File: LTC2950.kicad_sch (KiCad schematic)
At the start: 21 parts, among them SW1 SW_Push, U2 LTC2950ITS8-2_TRMPBF

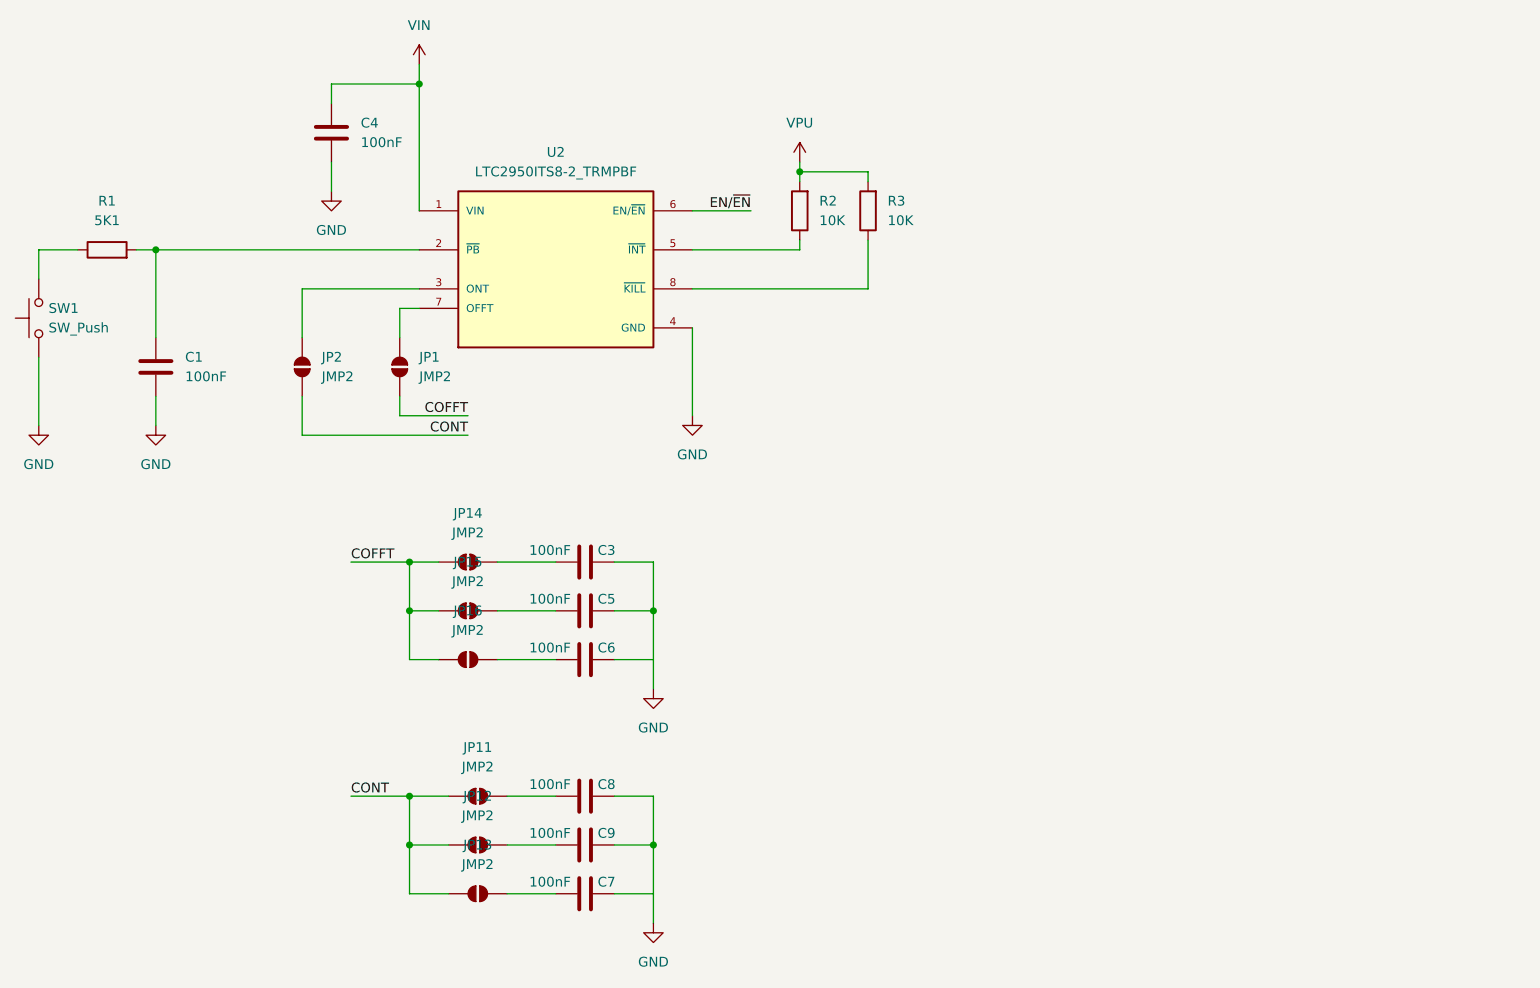
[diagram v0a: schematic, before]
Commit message: Added B.O.M, TODO: do PCB track layout
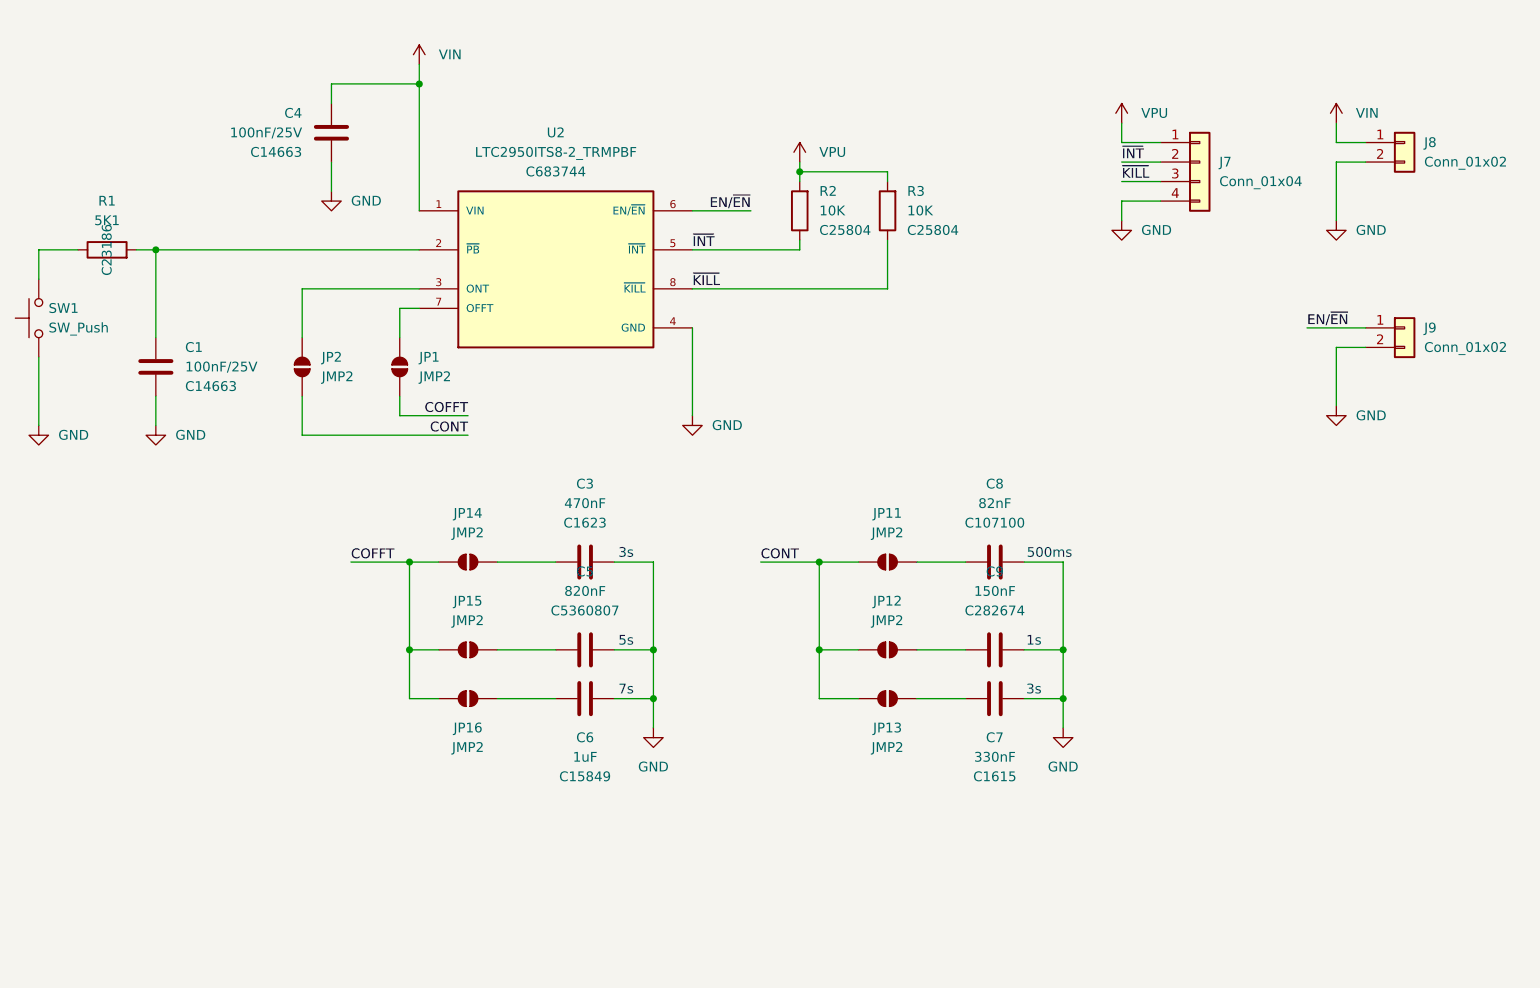
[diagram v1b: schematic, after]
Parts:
- added J7: Conn_01x04, Connector_PinHeader_2.54mm:PinHeader_1x04_P2.54mm_Vertical, symbol Connector_Generic:Conn_01x04
- added J8, J9: Conn_01x02, Connector_PinHeader_2.54mm:PinHeader_1x02_P2.54mm_Vertical, symbol Connector_Generic:Conn_01x02
- C1, C4: value 100nF -> 100nF/25V; JLCPCB Part # (none) -> C14663
- C3: value 100nF -> 470nF; JLCPCB Part # (none) -> C1623
- C5: value 100nF -> 820nF; JLCPCB Part # (none) -> C5360807
- C6: value 100nF -> 1uF; JLCPCB Part # (none) -> C15849
- C7: value 100nF -> 330nF; JLCPCB Part # (none) -> C1615
- C8: value 100nF -> 82nF; JLCPCB Part # (none) -> C107100
- C9: value 100nF -> 150nF; JLCPCB Part # (none) -> C282674
- R1: JLCPCB Part # (none) -> C23186
- R2, R3: JLCPCB Part # (none) -> C25804
- U2: JLCPCB Part # (none) -> C683744
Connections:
- net EN/~{EN}: now also J9.1 (Pin_1)
- net GND: now also C6.2, C7.2, J7.4 (Pin_4), J8.2 (Pin_2), J9.2 (Pin_2)
- net VIN: now also J8.1 (Pin_1)
- net VPU: now also J7.1 (Pin_1)
- net ~{INT}: now reaches R2.1, U2.5 (~{INT})
- net ~{INT}: now also J7.2 (Pin_2)
- net ~{KILL}: now reaches R3.1, U2.8 (~{KILL})
- net ~{KILL}: now also J7.3 (Pin_3)
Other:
- note added: "1s"
- note added: "3s"
- note added: "500ms"
- note added: "5s"
- note added: "7s"
- moved on the sheet: C5, C6, C7, C8, C9, JP11, JP12, JP13, JP15, JP16, R3

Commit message: Finished, 1st PCB order to JLCPCB
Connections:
- net VIN renamed VIN_2950
- net VPU renamed VPU_2950
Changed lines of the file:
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@@
 			)
 		)
-		(property "Value" "VPU"
+		(property "Value" "VPU_2950"
 			(at 224.79 59.6899 0)
 			(effects
@@
 			)
 		)
-		(property "Value" "VIN"
+		(property "Value" "VIN_2950"
 			(at 252.73 59.6899 0)
 			(effects
@@
 			)
 		)
-		(property "Value" "VIN"
+		(property "Value" "VIN_2950"
 			(at 133.35 52.0699 0)
 			(effects
@@
 		(fields_autoplaced yes)
 		(property "Reference" "R1"
+			(at 90.17 68.58 90)
+			(effects
+				(font
+					(size 1.27 1.27)
+				)
+			)
+		)
+		(property "Value" "5K1"
 			(at 90.17 71.12 90)
-			(effects
-				(font
-					(size 1.27 1.27)
-				)
-			)
-		)
-		(property "Value" "5K1"
-			(at 90.17 73.66 90)
 			(effects
 				(font
@@
 		)
 		(property "JLCPCB Part #" "C23186"
-			(at 90.17 77.47 0)
+			(at 90.17 73.66 90)
 			(effects
 				(font
@@
 			)
 		)
-		(property "Value" "VPU"
+		(property "Value" "VPU_2950"
 			(at 182.88 64.7699 0)
 			(effects
